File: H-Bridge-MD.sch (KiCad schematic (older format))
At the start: 67 parts, among them IC1 SI8650AB-B-IS1, IC2 A3921KLPTR-T, IC3 SI8650AB-B-IS1, IC4 A3921KLPTR-T, J1 Conn_01x02, J2 Conn_01x03, J3 Conn_01x05, J4 Conn_01x02, J5 Bus_mechaken_PCIexpress_x16_1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, Q1 NVMFD5C446NT1G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

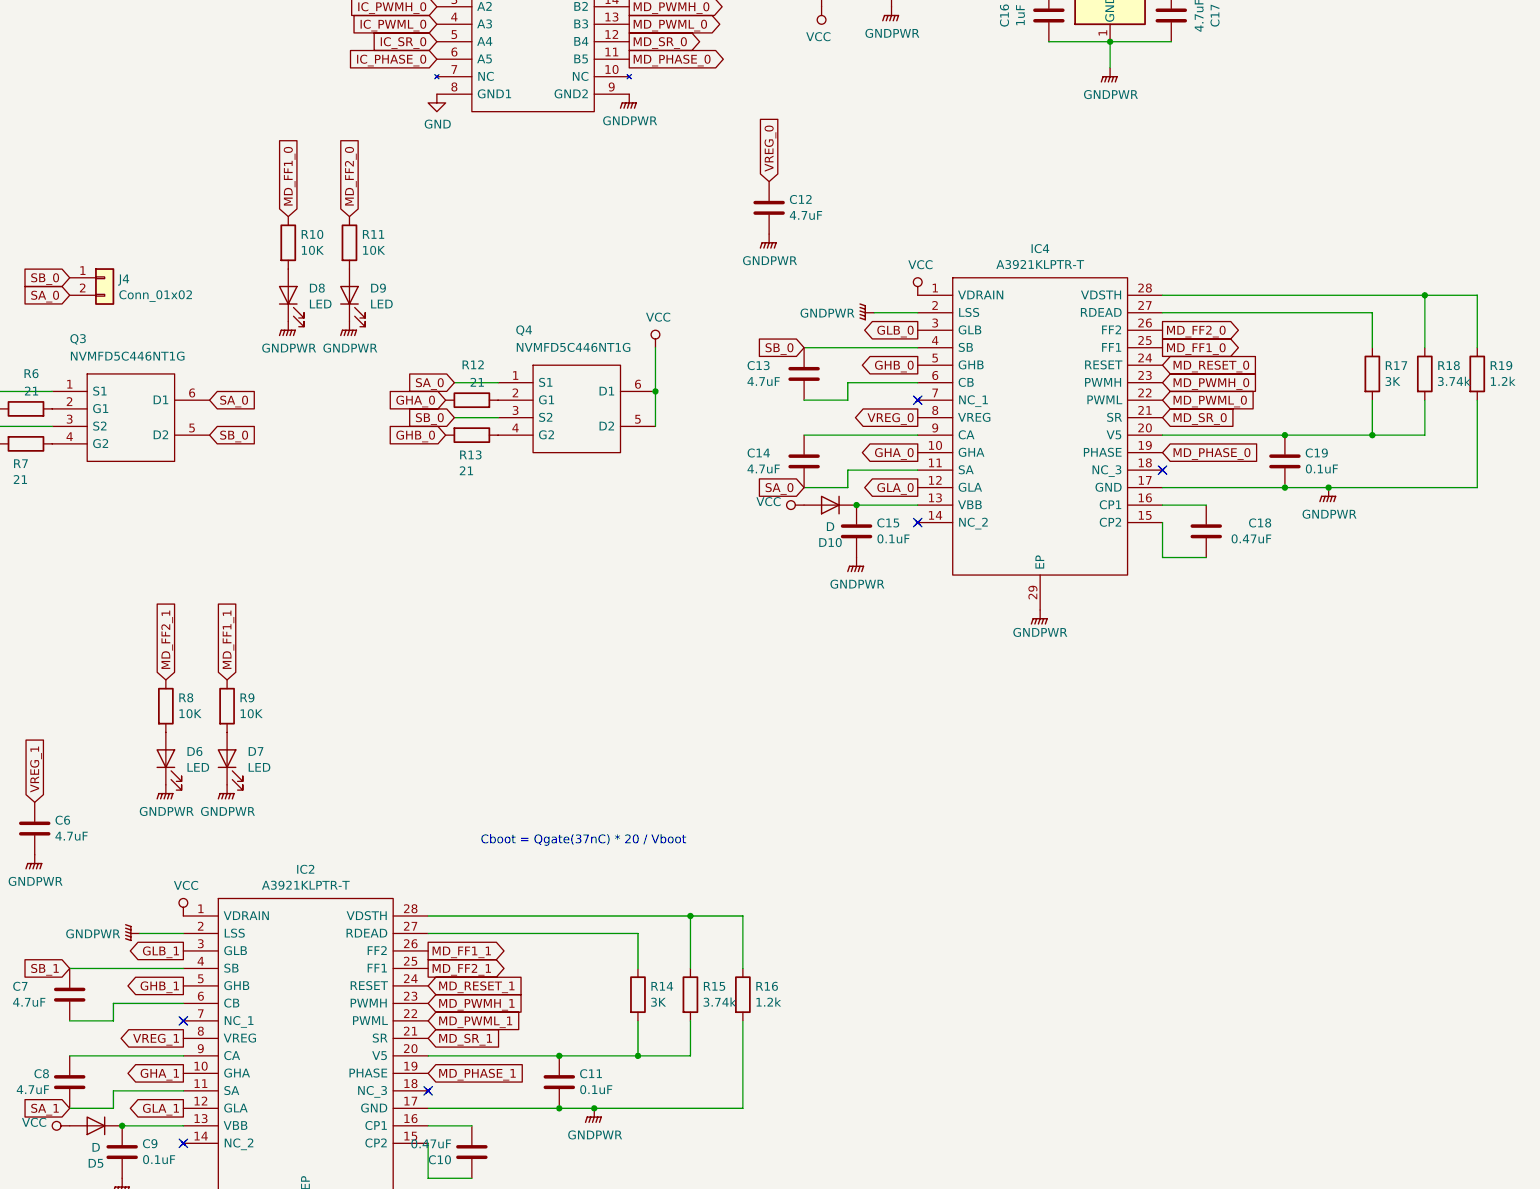
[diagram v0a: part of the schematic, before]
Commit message: fix
FF1&FF2 LED
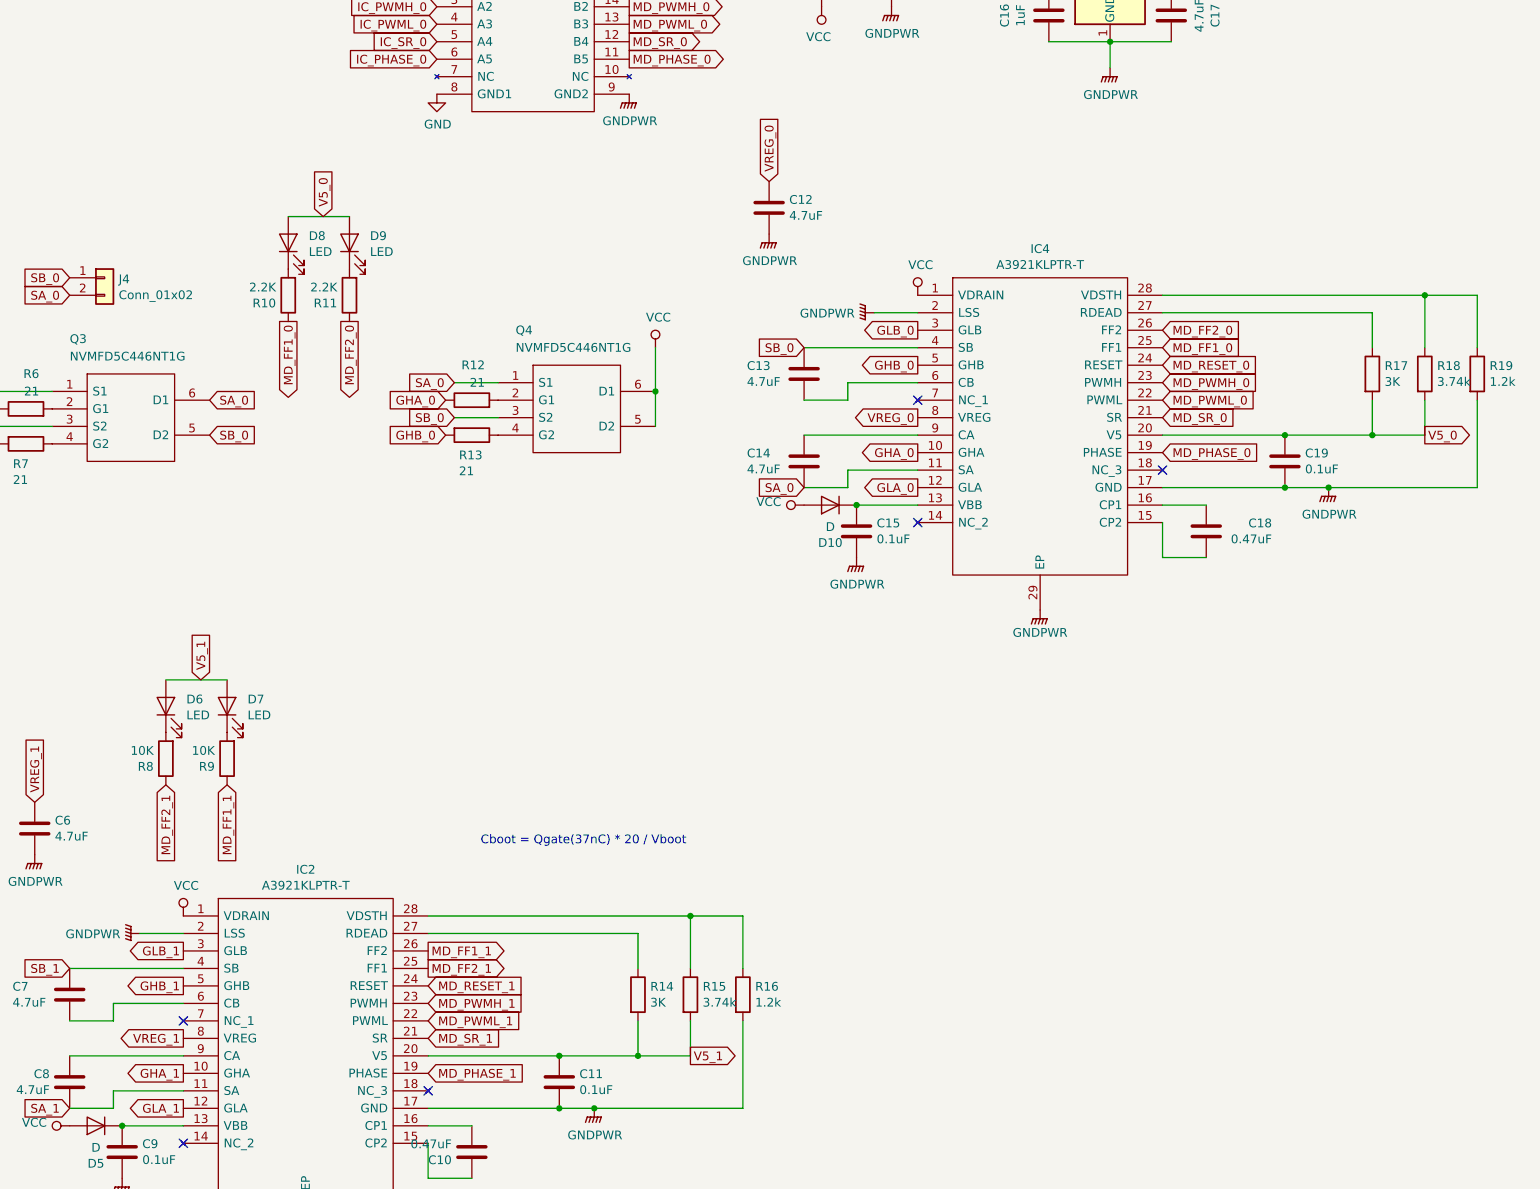
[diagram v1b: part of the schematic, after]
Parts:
- R10, R11: value 10K -> 2.2K
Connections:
- net GNDPWR: no longer D6.1 (K), D7.1 (K), D8.1 (K), D9.1 (K)
- net V5_1: now reaches C11.1, IC2.20 (V5), R14.2, R15.2
- net V5_1: now also D6.2 (A), D7.2 (A)
- net V5_0: now reaches C19.1, IC4.20 (V5), R17.2, R18.2
- net V5_0: now also D8.2 (A), D9.2 (A)
- net at R8.2: now also D6.1 (K); no longer D6.2 (A)
- net at R9.2: now also D7.1 (K); no longer D7.2 (A)
- net at R11.2: now also D9.1 (K); no longer D9.2 (A)
- net at R10.2: now also D8.1 (K); no longer D8.2 (A)
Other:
- moved on the sheet: D6, D7, D8, D9, R10, R11, R8, R9
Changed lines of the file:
@@
 Wire Wire Line
 	9100 10400 9850 10400
-Text GLabel 13300 6050 2    50   Output ~ 0
+Text GLabel 13300 6050 2    50   Input ~ 0
 MD_FF1_0
-Text GLabel 13300 5950 2    50   Output ~ 0
+Text GLabel 13300 5950 2    50   Input ~ 0
 MD_FF2_0
-Text GLabel 7950 7950 1    50   Input ~ 0
+Text GLabel 7950 8550 3    50   Input ~ 0
 MD_FF1_1
-Text GLabel 7600 7950 1    50   Input ~ 0
+Text GLabel 7600 8550 3    50   Input ~ 0
 MD_FF2_1
 Text GLabel 13500 4000 2    50   Output ~ 0
@@
 L Device:LED D6
 U 1 1 5DD0BADA
+P 7600 8100
+F 0 "D6" V 7639 7983 50  0000 R CNN
+F 1 "LED" V 7548 7983 50  0000 R CNN
+F 2 "LED_SMD:LED_0603_1608Metric" H 7600 8100 50  0001 C CNN
+F 3 "~" H 7600 8100 50  0001 C CNN
+	1    7600 8100
+	0    -1   -1   0
+$EndComp
+$Comp
+L Device:R R8
+U 1 1 5DD0BAE0
 P 7600 8400
-F 0 "D6" V 7639 8283 50  0000 R CNN
-F 1 "LED" V 7548 8283 50  0000 R CNN
-F 2 "LED_SMD:LED_0603_1608Metric" H 7600 8400 50  0001 C CNN
+F 0 "R8" H 7670 8446 50  0000 L CNN
+F 1 "10K" H 7670 8355 50  0000 L CNN
+F 2 "Resistor_SMD:R_0603_1608Metric" V 7530 8400 50  0001 C CNN
 F 3 "~" H 7600 8400 50  0001 C CNN
 	1    7600 8400
-	0    -1   -1   0
-$EndComp
-$Comp
-L Device:R R8
-U 1 1 5DD0BAE0
-P 7600 8100
-F 0 "R8" H 7670 8146 50  0000 L CNN
-F 1 "10K" H 7670 8055 50  0000 L CNN
-F 2 "Resistor_SMD:R_0603_1608Metric" V 7530 8100 50  0001 C CNN
-F 3 "~" H 7600 8100 50  0001 C CNN
-	1    7600 8100
-	1    0    0    -1
+	-1   0    0    1
 $EndComp
 $Comp
 L Device:LED D7
 U 1 1 5DD9DF80
+P 7950 8100
+F 0 "D7" V 7989 7983 50  0000 R CNN
+F 1 "LED" V 7898 7983 50  0000 R CNN
+F 2 "LED_SMD:LED_0603_1608Metric" H 7950 8100 50  0001 C CNN
+F 3 "~" H 7950 8100 50  0001 C CNN
+	1    7950 8100
+	0    -1   -1   0
+$EndComp
+$Comp
+L Device:R R9
+U 1 1 5DD9DF86
 P 7950 8400
-F 0 "D7" V 7989 8283 50  0000 R CNN
-F 1 "LED" V 7898 8283 50  0000 R CNN
-F 2 "LED_SMD:LED_0603_1608Metric" H 7950 8400 50  0001 C CNN
+F 0 "R9" H 8020 8446 50  0000 L CNN
+F 1 "10K" H 8020 8355 50  0000 L CNN
+F 2 "Resistor_SMD:R_0603_1608Metric" V 7880 8400 50  0001 C CNN
 F 3 "~" H 7950 8400 50  0001 C CNN
 	1    7950 8400
-	0    -1   -1   0
-$EndComp
-$Comp
-L Device:R R9
-U 1 1 5DD9DF86
-P 7950 8100
-F 0 "R9" H 8020 8146 50  0000 L CNN
-F 1 "10K" H 8020 8055 50  0000 L CNN
-F 2 "Resistor_SMD:R_0603_1608Metric" V 7880 8100 50  0001 C CNN
-F 3 "~" H 7950 8100 50  0001 C CNN
-	1    7950 8100
-	1    0    0    -1
-$EndComp
-$Comp
-L power:GNDPWR #PWR031
-U 1 1 5DF30A02
-P 7600 8550
-F 0 "#PWR031" H 7600 8350 50  0001 C CNN
-F 1 "GNDPWR" H 7604 8396 50  0000 C CNN
-F 2 "" H 7600 8500 50  0001 C CNN
-F 3 "" H 7600 8500 50  0001 C CNN
-	1    7600 8550
-	1    0    0    -1
-$EndComp
-$Comp
-L power:GNDPWR #PWR033
-U 1 1 5DF54F27
-P 7950 8550
-F 0 "#PWR033" H 7950 8350 50  0001 C CNN
-F 1 "GNDPWR" H 7954 8396 50  0000 C CNN
-F 2 "" H 7950 8500 50  0001 C CNN
-F 3 "" H 7950 8500 50  0001 C CNN
-	1    7950 8550
-	1    0    0    -1
-$EndComp
-Text GLabel 8300 5300 1    50   Input ~ 0
+	-1   0    0    1
+$EndComp
+Text GLabel 8300 5900 3    50   Output ~ 0
 MD_FF1_0
-Text GLabel 8650 5300 1    50   Input ~ 0
+Text GLabel 8650 5900 3    50   Output ~ 0
 MD_FF2_0
 $Comp
 L Device:LED D9
 U 1 1 5E145D00
+P 8650 5450
+F 0 "D9" V 8689 5333 50  0000 R CNN
+F 1 "LED" V 8598 5333 50  0000 R CNN
+F 2 "LED_SMD:LED_0603_1608Metric" H 8650 5450 50  0001 C CNN
+F 3 "~" H 8650 5450 50  0001 C CNN
+	1    8650 5450
+	0    -1   -1   0
+$EndComp
+$Comp
+L Device:R R11
+U 1 1 5E145D06
 P 8650 5750
-F 0 "D9" V 8689 5633 50  0000 R CNN
-F 1 "LED" V 8598 5633 50  0000 R CNN
-F 2 "LED_SMD:LED_0603_1608Metric" H 8650 5750 50  0001 C CNN
+F 0 "R11" H 8720 5796 50  0000 L CNN
+F 1 "2.2K" H 8720 5705 50  0000 L CNN
+F 2 "Resistor_SMD:R_0603_1608Metric" V 8580 5750 50  0001 C CNN
 F 3 "~" H 8650 5750 50  0001 C CNN
 	1    8650 5750
-	0    -1   -1   0
-$EndComp
-$Comp
-L Device:R R11
-U 1 1 5E145D06
-P 8650 5450
-F 0 "R11" H 8720 5496 50  0000 L CNN
-F 1 "10K" H 8720 5405 50  0000 L CNN
-F 2 "Resistor_SMD:R_0603_1608Metric" V 8580 5450 50  0001 C CNN
-F 3 "~" H 8650 5450 50  0001 C CNN
-	1    8650 5450
-	1    0    0    -1
+	-1   0    0    1
 $EndComp
 $Comp
 L Device:LED D8
 U 1 1 5E145D0C
-P 8300 5750
-F 0 "D8" V 8339 5633 50  0000 R CNN
-F 1 "LED" V 8248 5633 50  0000 R CNN
-F 2 "LED_SMD:LED_0603_1608Metric" H 8300 5750 50  0001 C CNN
-F 3 "~" H 8300 5750 50  0001 C CNN
-	1    8300 5750
-	0    -1   -1   0
-$EndComp
-$Comp
-L Device:R R10
-U 1 1 5E145D12
 P 8300 5450
-F 0 "R10" H 8370 5496 50  0000 L CNN
-F 1 "10K" H 8370 5405 50  0000 L CNN
-F 2 "Resistor_SMD:R_0603_1608Metric" V 8230 5450 50  0001 C CNN
+F 0 "D8" V 8339 5333 50  0000 R CNN
+F 1 "LED" V 8248 5333 50  0000 R CNN
+F 2 "LED_SMD:LED_0603_1608Metric" H 8300 5450 50  0001 C CNN
 F 3 "~" H 8300 5450 50  0001 C CNN
 	1    8300 5450
-	1    0    0    -1
-$EndComp
-$Comp
-L power:GNDPWR #PWR034
-U 1 1 5E145D18
-P 8300 5900
-F 0 "#PWR034" H 8300 5700 50  0001 C CNN
-F 1 "GNDPWR" H 8304 5746 50  0000 C CNN
-F 2 "" H 8300 5850 50  0001 C CNN
-F 3 "" H 8300 5850 50  0001 C CNN
-	1    8300 5900
-	1    0    0    -1
-$EndComp
-$Comp
-L power:GNDPWR #PWR036
-U 1 1 5E145D1E
-P 8650 5900
-F 0 "#PWR036" H 8650 5700 50  0001 C CNN
-F 1 "GNDPWR" H 8654 5746 50  0000 C CNN
-F 2 "" H 8650 5850 50  0001 C CNN
-F 3 "" H 8650 5850 50  0001 C CNN
-	1    8650 5900
-	1    0    0    -1
+	0    -1   -1   0
 $EndComp
 Wire Wire Line
@@
 	1    0    0    -1
 $EndComp
+$Comp
+L Device:R R10
+U 1 1 5E145D12
+P 8300 5750
+F 0 "R10" H 8370 5796 50  0000 L CNN
+F 1 "2.2K" H 8370 5705 50  0000 L CNN
+F 2 "Resistor_SMD:R_0603_1608Metric" V 8230 5750 50  0001 C CNN
+F 3 "~" H 8300 5750 50  0001 C CNN
+	1    8300 5750
+	-1   0    0    1
+$EndComp
+Text GLabel 14800 6550 2    50   Output ~ 0
+V5_0
+Text GLabel 8500 5300 1    50   Input ~ 0
+V5_0
+Wire Wire Line
+	8300 5300 8650 5300
+Text GLabel 10600 10100 2    50   Output ~ 0
+V5_1
+Text GLabel 7800 7950 1    50   Input ~ 0
+V5_1
+Wire Wire Line
+	7600 7950 7950 7950
 $EndSCHEMATC
